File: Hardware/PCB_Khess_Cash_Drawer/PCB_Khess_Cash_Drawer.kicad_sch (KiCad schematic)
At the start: 17 parts, among them J1 Screw_Terminal_01x02, J2 Conn_01x02, J3 RJ11_Connector, J4 USB3_A, Q1 BUK9637-100E,118, U1 R-78B5.0-2.0

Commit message: fix: fix pcb
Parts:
- removed J2: Conn_01x02, Connector_PinHeader_2.54mm:PinHeader_1x02_P2.54mm_Vertical, symbol Connector_Generic:Conn_01x02
- removed J4: USB3_A, Connector_USB:USB3_A_Molex_48406-0001_Horizontal_Stacked, symbol Connector:USB3_A
- removed PS1: HLK-PM12, Converter_ACDC:Converter_ACDC_Hi-Link_HLK-PMxx, symbol Converter_ACDC:HLK-PM12
- added C4: 100u, Capacitor_SMD:CP_Elec_8x10, symbol Device:C_Polarized
- added C5: 1u, Capacitor_SMD:C_0805_2012Metric, symbol Device:C
- added D2: D_TVS, Diode_SMD:D_SMA_Handsoldering, symbol Device:D_TVS
- added F1: Fuse, Fuse:Fuseholder_Cylinder-5x20mm_Schurter_0031_8201_Horizontal_Open, symbol Device:Fuse
- added J2: Conn_01x03, Connector_PinHeader_2.54mm:PinHeader_1x03_P2.54mm_Horizontal, symbol Connector_Generic:Conn_01x03
- added PS2: PSK-15E-12, PSK-15E-12:CONV_PSK-15E-12, symbol TP5100:PSK-15E-12
- added R3: 6.8, Resistor_SMD:R_2512_6332Metric_Pad1.40x3.35mm_HandSolder, symbol Device:R
- added RV1: 10D561K, MOV-10D561K:VAR_MOV-10D561K, symbol Device:Varistor
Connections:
- net +12V: now also C4.1, C5.1, D2.2 (A2), PS2.4 (+VO)
- net +5V: now also J2.1 (Pin_1)
- net AC_LINE: now also F1.1
- net AC_NEUTRAL: now also PS2.1 (AC(N)), RV1.2
- net GND: now also C4.2, C5.2, D2.1 (A1), J2.3 (Pin_3), PS2.5 (-VO)
- net GPIO_CONTROL: now also J2.2 (Pin_2)
- new net AC_LINE_FUSE: F1.2, R3.1, RV1.1
- new net AC_LINE_FUSE_R: PS2.2 (AC(L)), R3.2
- no-connect marks 12 -> 4
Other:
- moved on the sheet: J1, J3

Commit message: review schematics
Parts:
- C2: value 4.7u -> 4u7
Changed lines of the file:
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@@
 		)
 		(instances
-			(project "PCB_Khess"
+			(project "PCB_Khess_Cash_Drawer"
 				(path "/e7800f41-69a9-4114-9938-e2f8d3e5043e"
 					(reference "#PWR012")
@@
 		)
 		(instances
-			(project "PCB_Khess"
+			(project "PCB_Khess_Cash_Drawer"
 				(path "/e7800f41-69a9-4114-9938-e2f8d3e5043e"
 					(reference "H4")
@@
 		)
 		(instances
-			(project ""
+			(project "PCB_Khess_Cash_Drawer"
 				(path "/e7800f41-69a9-4114-9938-e2f8d3e5043e"
 					(reference "Q1")
@@
 		)
 		(instances
-			(project "PCB_Khess"
+			(project "PCB_Khess_Cash_Drawer"
 				(path "/e7800f41-69a9-4114-9938-e2f8d3e5043e"
 					(reference "R2")
@@
 		)
 		(instances
-			(project ""
+			(project "PCB_Khess_Cash_Drawer"
 				(path "/e7800f41-69a9-4114-9938-e2f8d3e5043e"
 					(reference "D2")
@@
 		)
 		(instances
-			(project ""
+			(project "PCB_Khess_Cash_Drawer"
 				(path "/e7800f41-69a9-4114-9938-e2f8d3e5043e"
 					(reference "J3")
@@
 		)
 		(instances
-			(project "PCB_Khess"
+			(project "PCB_Khess_Cash_Drawer"
 				(path "/e7800f41-69a9-4114-9938-e2f8d3e5043e"
 					(reference "#PWR07")
@@
 		)
 		(instances
-			(project ""
+			(project "PCB_Khess_Cash_Drawer"
 				(path "/e7800f41-69a9-4114-9938-e2f8d3e5043e"
 					(reference "J1")
@@
 		)
 		(instances
-			(project "PCB_Khess"
+			(project "PCB_Khess_Cash_Drawer"
 				(path "/e7800f41-69a9-4114-9938-e2f8d3e5043e"
 					(reference "#PWR02")
@@
 		)
 		(instances
-			(project ""
+			(project "PCB_Khess_Cash_Drawer"
 				(path "/e7800f41-69a9-4114-9938-e2f8d3e5043e"
 					(reference "PS2")
@@
 		)
 		(instances
-			(project ""
+			(project "PCB_Khess_Cash_Drawer"
 				(path "/e7800f41-69a9-4114-9938-e2f8d3e5043e"
 					(reference "#FLG01")
@@
 		)
 		(instances
-			(project "PCB_Khess"
+			(project "PCB_Khess_Cash_Drawer"
 				(path "/e7800f41-69a9-4114-9938-e2f8d3e5043e"
 					(reference "H2")
@@
 		)
 		(instances
-			(project ""
+			(project "PCB_Khess_Cash_Drawer"
 				(path "/e7800f41-69a9-4114-9938-e2f8d3e5043e"
 					(reference "#PWR06")
@@
 		)
 		(instances
-			(project ""
+			(project "PCB_Khess_Cash_Drawer"
 				(path "/e7800f41-69a9-4114-9938-e2f8d3e5043e"
 					(reference "L1")
@@
 		)
 		(instances
-			(project "PCB_Khess"
+			(project "PCB_Khess_Cash_Drawer"
 				(path "/e7800f41-69a9-4114-9938-e2f8d3e5043e"
 					(reference "#PWR021")
@@
 		)
 		(instances
-			(project ""
+			(project "PCB_Khess_Cash_Drawer"
 				(path "/e7800f41-69a9-4114-9938-e2f8d3e5043e"
 					(reference "C4")
@@
 		)
 		(instances
-			(project ""
+			(project "PCB_Khess_Cash_Drawer"
 				(path "/e7800f41-69a9-4114-9938-e2f8d3e5043e"
 					(reference "U1")
@@
 		)
 		(instances
-			(project ""
+			(project "PCB_Khess_Cash_Drawer"
 				(path "/e7800f41-69a9-4114-9938-e2f8d3e5043e"
 					(reference "#PWR01")
@@
 		)
 		(instances
-			(project ""
+			(project "PCB_Khess_Cash_Drawer"
 				(path "/e7800f41-69a9-4114-9938-e2f8d3e5043e"
 					(reference "R3")
@@
 		)
 		(instances
-			(project ""
+			(project "PCB_Khess_Cash_Drawer"
 				(path "/e7800f41-69a9-4114-9938-e2f8d3e5043e"
 					(reference "F1")
@@
 			)
 		)
-		(property "Value" "4.7u"
+		(property "Value" "4u7"
 			(at 43.18 36.8362 0)
 			(effects
@@
 		)
 		(instances
-			(project "PCB_Khess"
+			(project "PCB_Khess_Cash_Drawer"
 				(path "/e7800f41-69a9-4114-9938-e2f8d3e5043e"
 					(reference "C2")
@@
 		)
 		(instances
-			(project ""
+			(project "PCB_Khess_Cash_Drawer"
 				(path "/e7800f41-69a9-4114-9938-e2f8d3e5043e"
 					(reference "J2")
@@
 		)
 		(instances
-			(project ""
+			(project "PCB_Khess_Cash_Drawer"
 				(path "/e7800f41-69a9-4114-9938-e2f8d3e5043e"
 					(reference "RV1")
@@
 		)
 		(instances
-			(project ""
+			(project "PCB_Khess_Cash_Drawer"
 				(path "/e7800f41-69a9-4114-9938-e2f8d3e5043e"
 					(reference "R1")
@@
 		)
 		(instances
-			(project ""
+			(project "PCB_Khess_Cash_Drawer"
 				(path "/e7800f41-69a9-4114-9938-e2f8d3e5043e"
 					(reference "C1")
@@
 		)
 		(instances
-			(project "PCB_Khess"
+			(project "PCB_Khess_Cash_Drawer"
 				(path "/e7800f41-69a9-4114-9938-e2f8d3e5043e"
 					(reference "#PWR03")
@@
 		)
 		(instances
-			(project "PCB_Khess"
+			(project "PCB_Khess_Cash_Drawer"
 				(path "/e7800f41-69a9-4114-9938-e2f8d3e5043e"
 					(reference "H1")
@@
 		)
 		(instances
-			(project ""
+			(project "PCB_Khess_Cash_Drawer"
 				(path "/e7800f41-69a9-4114-9938-e2f8d3e5043e"
 					(reference "#PWR04")
@@
 		)
 		(instances
-			(project "PCB_Khess"
+			(project "PCB_Khess_Cash_Drawer"
 				(path "/e7800f41-69a9-4114-9938-e2f8d3e5043e"
 					(reference "#PWR013")
@@
 		)
 		(instances
-			(project ""
+			(project "PCB_Khess_Cash_Drawer"
 				(path "/e7800f41-69a9-4114-9938-e2f8d3e5043e"
 					(reference "C5")
@@
 		)
 		(instances
-			(project "PCB_Khess"
+			(project "PCB_Khess_Cash_Drawer"
 				(path "/e7800f41-69a9-4114-9938-e2f8d3e5043e"
 					(reference "H3")
@@
 		)
 		(instances
-			(project ""
+			(project "PCB_Khess_Cash_Drawer"
 				(path "/e7800f41-69a9-4114-9938-e2f8d3e5043e"
 					(reference "D1")

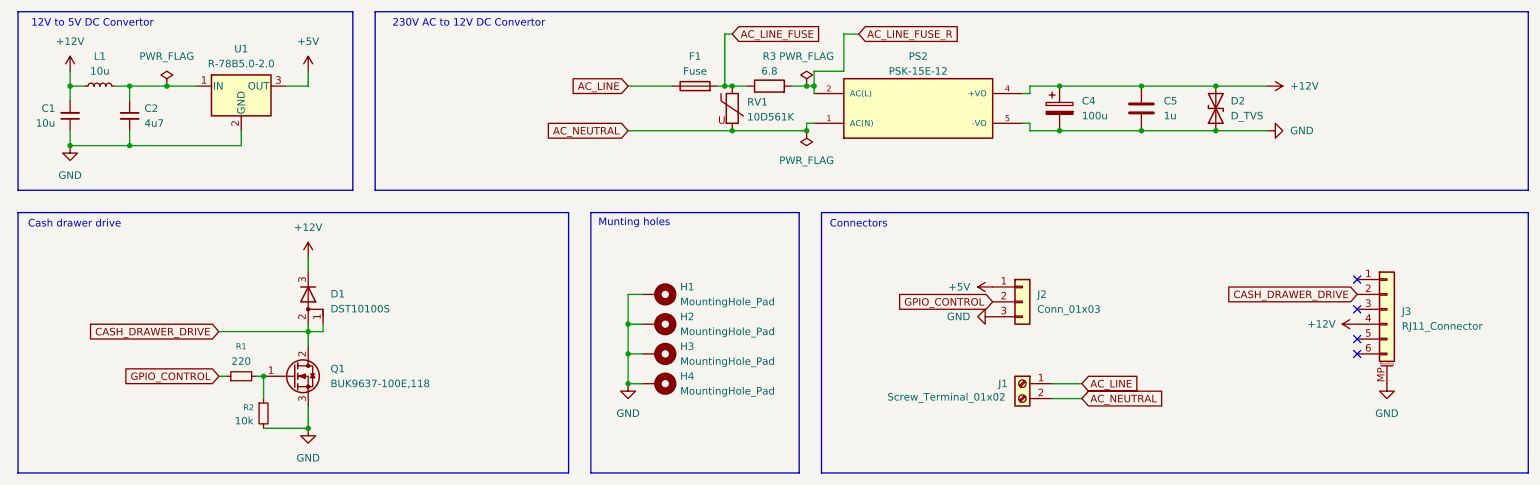
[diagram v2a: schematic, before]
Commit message: fix: update schematic
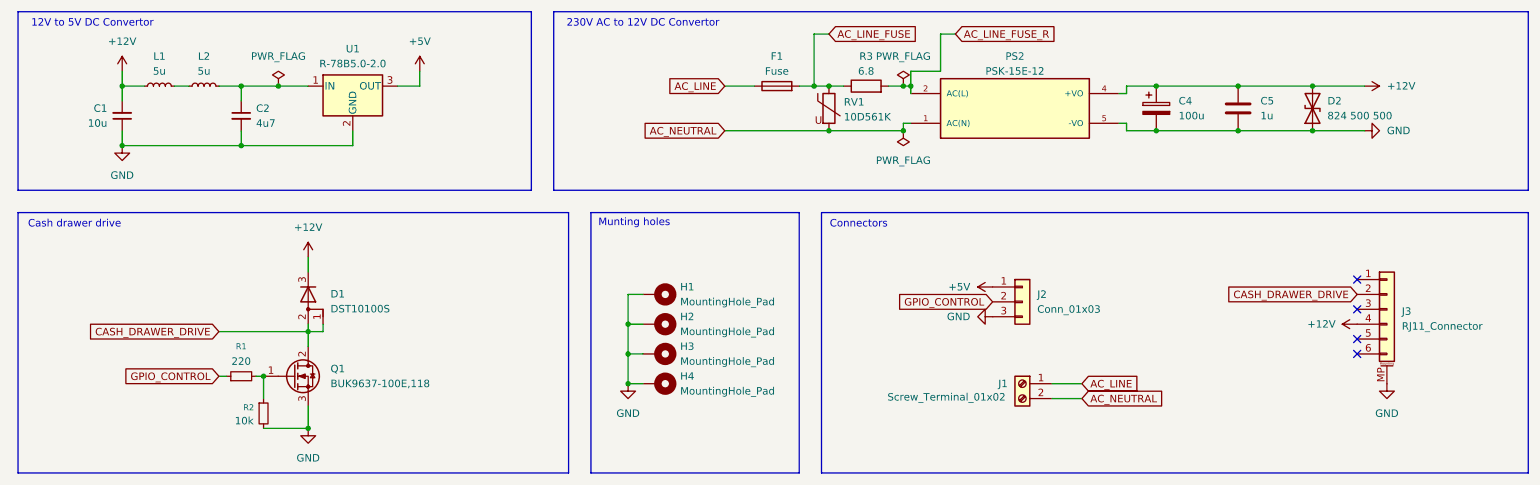
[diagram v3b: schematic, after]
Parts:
- added L2: 5u, Inductor_SMD:L_10.4x10.4_H4.8, symbol Device:L_Small
- C1: footprint Capacitor_SMD:C_0603_1608Metric_Pad1.08x0.95mm_HandSolder -> Capacitor_SMD:CP_Elec_4x5.4
- C2: footprint Capacitor_SMD:C_0603_1608Metric_Pad1.08x0.95mm_HandSolder -> Capacitor_SMD:CP_Elec_5x5.4
- C4: footprint Capacitor_SMD:CP_Elec_8x10 -> Capacitor_SMD:CP_Elec_6.3x7.7
- C5: footprint Capacitor_SMD:C_0805_2012Metric -> Capacitor_SMD:CP_Elec_4x5.4
- D2: value D_TVS -> 824 500 500; footprint Diode_SMD:D_SMA_Handsoldering -> Diode_SMD:D_SMA
- L1: value 10u -> 5u; footprint Inductor_SMD:L_0603_1608Metric_Pad1.05x0.95mm_HandSolder -> Inductor_SMD:L_10.4x10.4_H4.8
- R3: footprint Resistor_SMD:R_2512_6332Metric_Pad1.40x3.35mm_HandSolder -> Resistor_THT:R_Axial_DIN0516_L15.5mm_D5.0mm_P20.32mm_Horizontal
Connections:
- net at C2.1, U1.1 (IN): now also L2.2; no longer L1.2
- new net: L1.2, L2.1
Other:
- moved on the sheet: C1, C2, C4, C5, D2, F1, L1, PS2, R3, RV1, U1

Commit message: fix: update two pcb and add gnd via
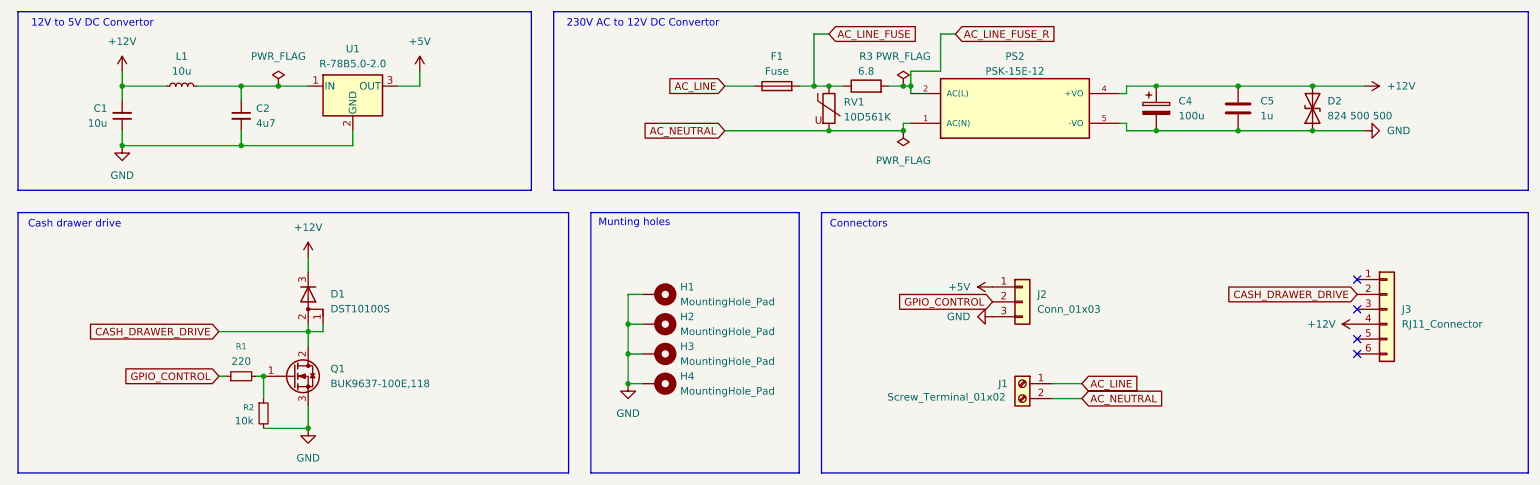
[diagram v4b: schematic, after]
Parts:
- removed J3: RJ11_Connector, Connector_RJ:RJ12_Amphenol_54601-x06_Horizontal, symbol Connector_Generic_MountingPin:Conn_01x06_MountingPin
- removed L2: 5u, Inductor_SMD:L_10.4x10.4_H4.8, symbol Device:L_Small
- added J3: RJ11_Connector, Connector_RJ:RJ12_Amphenol_54601-x06_Horizontal, symbol Connector_Generic:Conn_01x06
- C1, C5: footprint Capacitor_SMD:CP_Elec_4x5.4 -> Capacitor_SMD:C_0805_2012Metric
- C2: footprint Capacitor_SMD:CP_Elec_5x5.4 -> Capacitor_SMD:C_0805_2012Metric
- J2: footprint Connector_PinHeader_2.54mm:PinHeader_1x03_P2.54mm_Horizontal -> Connector_PinHeader_2.54mm:PinHeader_1x03_P2.54mm_Vertical
- L1: value 5u -> 10u; footprint Inductor_SMD:L_10.4x10.4_H4.8 -> Inductor_SMD:L_0805_2012Metric
- R1, R2: footprint Resistor_SMD:R_0603_1608Metric_Pad0.98x0.95mm_HandSolder -> Resistor_SMD:R_0603_1608Metric
- R3: footprint Resistor_THT:R_Axial_DIN0516_L15.5mm_D5.0mm_P20.32mm_Horizontal -> Resistor_THT:R_Axial_DIN0414_L11.9mm_D4.5mm_P20.32mm_Horizontal
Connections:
- net +12V: now also J3.4 (Pin_4)
- net CASH_DRAWER_DRIVE: now also J3.2 (Pin_2)
- net at L1.2: now also C2.1, U1.1 (IN)
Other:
- moved on the sheet: L1
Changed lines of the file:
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@@
 	(wire
 		(pts
-			(xy 39.37 30.48) (xy 43.18 30.48)
+			(xy 39.37 30.48) (xy 46.99 30.48)
 		)
 		(stroke
@@
 	(wire
 		(pts
-			(xy 55.88 30.48) (xy 59.69 30.48)
-		)
-		(stroke
-			(width 0)
-			(type default)
-		)
-	)
-	(wire
-		(pts
-			(xy 50.8 30.48) (xy 48.26 30.48)
+			(xy 52.07 30.48) (xy 59.69 30.48)
 		)
 		(stroke
@@
 			)
 		)
-		(property "Footprint" "Resistor_SMD:R_0603_1608Metric_Pad0.98x0.95mm_HandSolder"
+		(property "Footprint" "Resistor_SMD:R_0603_1608Metric"
 			(at 63.5 86.36 0)
 			(effects
@@
 				(path "/e7800f41-69a9-4114-9938-e2f8d3e5043e"
 					(reference "D2")
-					(unit 1)
-				)
-			)
-		)
-	)
-	(symbol
-		(lib_id "Connector_Generic_MountingPin:Conn_01x06_MountingPin")
-		(at 255.27 68.58 0)
-		(unit 1)
-		(exclude_from_sim no)
-		(in_bom yes)
-		(on_board yes)
-		(dnp no)
-		(fields_autoplaced yes)
-		(property "Reference" "J3"
-			(at 257.81 68.9355 0)
-			(effects
-				(font
-					(size 1.27 1.27)
-				)
-				(justify left)
-			)
-		)
-		(property "Value" "RJ11_Connector"
-			(at 257.81 71.4755 0)
-			(effects
-				(font
-					(size 1.27 1.27)
-				)
-				(justify left)
-			)
-		)
-		(property "Footprint" "Connector_RJ:RJ12_Amphenol_54601-x06_Horizontal"
-			(at 255.27 68.58 0)
-			(effects
-				(font
-					(size 1.27 1.27)
-				)
-				(hide yes)
-			)
-		)
-		(property "Datasheet" "~"
-			(at 255.27 68.58 0)
-			(effects
-				(font
-					(size 1.27 1.27)
-				)
-				(hide yes)
-			)
-		)
-		(property "Description" "Generic connectable mounting pin connector, single row, 01x06, script generated (kicad-library-utils/schlib/autogen/connector/)"
-			(at 255.27 68.58 0)
-			(effects
-				(font
-					(size 1.27 1.27)
-				)
-				(hide yes)
-			)
-		)
-		(pin "1"
-		)
-		(pin "3"
-		)
-		(pin "2"
-		)
-		(pin "6"
-		)
-		(pin "4"
-		)
-		(pin "5"
-		)
-		(pin "MP"
-		)
-		(instances
-			(project "PCB_Khess_Cash_Drawer"
-				(path "/e7800f41-69a9-4114-9938-e2f8d3e5043e"
-					(reference "J3")
 					(unit 1)
 				)
@@
 	)
 	(symbol
-		(lib_id "power:GND")
-		(at 255.27 81.28 0)
-		(unit 1)
-		(exclude_from_sim no)
-		(in_bom yes)
-		(on_board yes)
-		(dnp no)
-		(fields_autoplaced yes)
-		(property "Reference" "#PWR02"
-			(at 255.27 87.63 0)
-			(effects
-				(font
-					(size 1.27 1.27)
-				)
-				(hide yes)
-			)
-		)
-		(property "Value" "GND"
-			(at 255.27 86.36 0)
-			(effects
-				(font
-					(size 1.27 1.27)
-				)
-			)
-		)
-		(property "Footprint" ""
-			(at 255.27 81.28 0)
-			(effects
-				(font
-					(size 1.27 1.27)
-				)
-				(hide yes)
-			)
-		)
-		(property "Datasheet" ""
-			(at 255.27 81.28 0)
-			(effects
-				(font
-					(size 1.27 1.27)
-				)
-				(hide yes)
-			)
-		)
-		(property "Description" "Power symbol creates a global label with name \"GND\" , ground"
-			(at 255.27 81.28 0)
-			(effects
-				(font
-					(size 1.27 1.27)
-				)
-				(hide yes)
-			)
-		)
-		(pin "1"
-		)
-		(instances
-			(project "PCB_Khess_Cash_Drawer"
-				(path "/e7800f41-69a9-4114-9938-e2f8d3e5043e"
-					(reference "#PWR02")
-					(unit 1)
-				)
-			)
-		)
-	)
-	(symbol
 		(lib_id "TP5100:PSK-15E-12")
 		(at 191.77 34.29 0)
@@
 	)
 	(symbol
+		(lib_id "Connector_Generic:Conn_01x06")
+		(at 255.27 68.58 0)
+		(unit 1)
+		(exclude_from_sim no)
+		(in_bom yes)
+		(on_board yes)
+		(dnp no)
+		(fields_autoplaced yes)
+		(property "Reference" "J3"
+			(at 257.81 68.5799 0)
+			(effects
+				(font
+					(size 1.27 1.27)
+				)
+				(justify left)
+			)
+		)
+		(property "Value" "RJ11_Connector"
+			(at 257.81 71.1199 0)
+			(effects
+				(font
+					(size 1.27 1.27)
+				)
+				(justify left)
+			)
+		)
+		(property "Footprint" "Connector_RJ:RJ12_Amphenol_54601-x06_Horizontal"
+			(at 255.27 68.58 0)
+			(effects
+				(font
+					(size 1.27 1.27)
+				)
+				(hide yes)
+			)
+		)
+		(property "Datasheet" "~"
+			(at 255.27 68.58 0)
+			(effects
+				(font
+					(size 1.27 1.27)
+				)
+				(hide yes)
+			)
+		)
+		(property "Description" "Generic connector, single row, 01x06, script generated (kicad-library-utils/schlib/autogen/connector/)"
+			(at 255.27 68.58 0)
+			(effects
+				(font
+					(size 1.27 1.27)
+				)
+				(hide yes)
+			)
+		)
+		(pin "1"
+		)
+		(pin "3"
+		)
+		(pin "5"
+		)
+		(pin "6"
+		)
+		(pin "2"
+		)
+		(pin "4"
+		)
+		(instances
+			(project ""
+				(path "/e7800f41-69a9-4114-9938-e2f8d3e5043e"
+					(reference "J3")
+					(unit 1)
+				)
+			)
+		)
+	)
+	(symbol
 		(lib_id "power:PWR_FLAG")
 		(at 66.04 30.48 0)
@@
 	(symbol
 		(lib_id "Device:L_Small")
-		(at 45.72 30.48 90)
+		(at 49.53 30.48 90)
 		(unit 1)
 		(exclude_from_sim no)
@@
 		(fields_autoplaced yes)
 		(property "Reference" "L1"
-			(at 45.72 25.4 90)
-			(effects
-				(font
-					(size 1.27 1.27)
-				)
-			)
-		)
-		(property "Value" "5u"
-			(at 45.72 27.94 90)
-			(effects
-				(font
-					(size 1.27 1.27)
-				)
-			)
-		)
-		(property "Footprint" "Inductor_SMD:L_10.4x10.4_H4.8"
-			(at 45.72 30.48 0)
+			(at 49.53 25.4 90)
+			(effects
+				(font
+					(size 1.27 1.27)
+				)
+			)
+		)
+		(property "Value" "10u"
+			(at 49.53 27.94 90)
+			(effects
+				(font
+					(size 1.27 1.27)
+				)
+			)
+		)
+		(property "Footprint" "Inductor_SMD:L_0805_2012Metric"
+			(at 49.53 30.48 0)
 			(effects
 				(font
@@
 		)
 		(property "Datasheet" "~"
-			(at 45.72 30.48 0)
+			(at 49.53 30.48 0)
 			(effects
 				(font
@@
 		)
 		(property "Description" "Inductor, small symbol"
-			(at 45.72 30.48 0)
+			(at 49.53 30.48 0)
 			(effects
 				(font
@@
 			)
 		)
-		(property "Footprint" "Resistor_THT:R_Axial_DIN0516_L15.5mm_D5.0mm_P20.32mm_Horizontal"
+		(property "Footprint" "Resistor_THT:R_Axial_DIN0414_L11.9mm_D4.5mm_P20.32mm_Horizontal"
 			(at 166.37 32.258 90)
 			(effects
@@
 			)
 		)
-		(property "Datasheet" "~"
+		(property "Datasheet" "https://www.vishay.com/docs/28730/ac_ac-at_ac-ni.pdf"
 			(at 166.37 30.48 0)
 			(effects
@@
 			)
 		)
-		(property "Footprint" "Capacitor_SMD:CP_Elec_5x5.4"
+		(property "Footprint" "Capacitor_SMD:C_0805_2012Metric"
 			(at 59.69 35.56 0)
 			(effects
@@
 			)
 		)
-		(property "Footprint" "Connector_PinHeader_2.54mm:PinHeader_1x03_P2.54mm_Horizontal"
+		(property "Footprint" "Connector_PinHeader_2.54mm:PinHeader_1x03_P2.54mm_Vertical"
 			(at 193.04 67.31 0)
 			(effects
@@
 			)
 		)
-		(property "Footprint" "Resistor_SMD:R_0603_1608Metric_Pad0.98x0.95mm_HandSolder"
+		(property "Footprint" "Resistor_SMD:R_0603_1608Metric"
 			(at 59.69 80.01 0)
 			(effects
@@
 			)
 		)
-		(property "Footprint" "Capacitor_SMD:CP_Elec_4x5.4"
+		(property "Footprint" "Capacitor_SMD:C_0805_2012Metric"
 			(at 39.37 35.56 0)
 			(effects
@@
 			)
 		)
-		(property "Footprint" "Capacitor_SMD:CP_Elec_4x5.4"
+		(property "Footprint" "Capacitor_SMD:C_0805_2012Metric"
 			(at 230.8352 38.1 0)
 			(effects
@@
 					(unit 1)
 				)
-			)
-		)
-	)
-	(symbol
-		(lib_id "Device:L_Small")
-		(at 53.34 30.48 90)
-		(unit 1)
-		(exclude_from_sim no)
-		(in_bom yes)
-		(on_board yes)
-		(dnp no)
-		(fields_autoplaced yes)
-		(property "Reference" "L2"
-			(at 53.34 25.4 90)
-			(effects
-				(font
-					(size 1.27 1.27)
-				)
-			)
-		)
-		(property "Value" "5u"
-			(at 53.34 27.94 90)
-			(effects
-				(font
-					(size 1.27 1.27)
-				)
-			)
-		)
-		(property "Footprint" "Inductor_SMD:L_10.4x10.4_H4.8"
-			(at 53.34 30.48 0)
-			(effects
-				(font
-					(size 1.27 1.27)
-				)
-				(hide yes)
-			)
-		)
-		(property "Datasheet" "~"
-			(at 53.34 30.48 0)
-			(effects
-				(font
-					(size 1.27 1.27)
-				)
-				(hide yes)
-			)
-		)
-		(property "Description" "Inductor, small symbol"
-			(at 53.34 30.48 0)
-			(effects
-				(font
-					(size 1.27 1.27)
-				)
-				(hide yes)
-			)
-		)
-		(pin "2"
-		)
-		(pin "1"
-		)
-		(instances
-			(project "PCB_Khess_Cash_Drawer"
-				(path "/e7800f41-69a9-4114-9938-e2f8d3e5043e"
-					(reference "L2")
-					(unit 1)
-				)

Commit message: fix
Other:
- company: (none) -> ENSEA
- title: PCB K'Hess -> PCB Khess_Cash_Drawer
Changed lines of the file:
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@@
 	(paper "A4")
 	(title_block
-		(title "PCB K'Hess")
+		(title "PCB Khess_Cash_Drawer")
+		(date "2026-05-19")
 		(rev "1.0")
+		(company "ENSEA")
+		(comment 1 "Estelle Zhang / Clément Jouneau / Rim Bouchikhi")
+		(comment 2 "Bryan-Sowanna Ing / Naïm Kirmat / Margaux Laplante / Rayan Laghouane")
 	)
 	(rectangle
